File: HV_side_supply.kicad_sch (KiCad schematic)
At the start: 34 parts, among them U103 LM217MDT, U104 LM217MDT

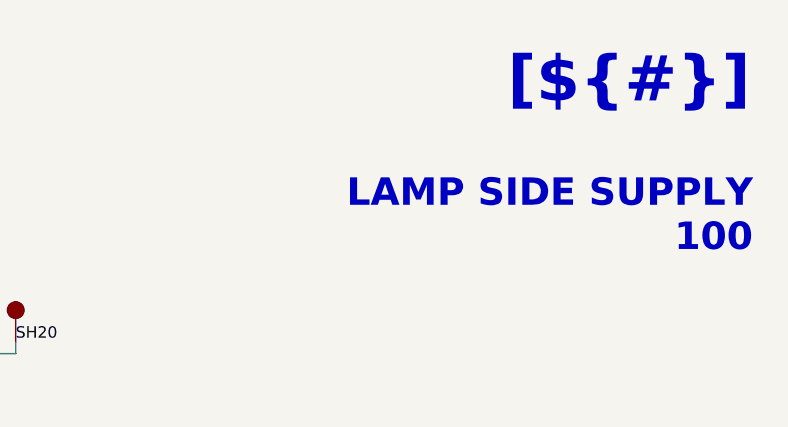
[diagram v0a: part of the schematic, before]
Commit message: Reworked sheet titles
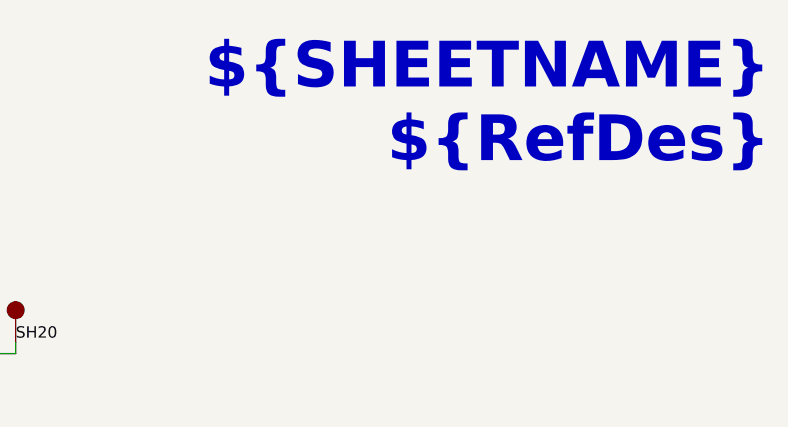
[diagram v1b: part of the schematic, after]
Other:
- note removed: "LAMP SIDE SUPPLY 100"
- title: (none) -> ${SHEETNAME}
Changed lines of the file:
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@@
 	(paper "A4")
 	(title_block
+		(title "${SHEETNAME}")
 		(date "2025-01-12")
 	)
@@
 		)
 	)
-	(text "LAMP SIDE SUPPLY\n100"
+	(text_box "${SHEETNAME}\n${RefDes}"
 		(exclude_from_sim no)
-		(at 277.495 35.56 0)
-		(effects
-			(font
-				(size 3.048 3.048)
-				(thickness 0.4064)
-				(bold yes)
-				(color 0 0 255 1)
-			)
-			(justify right)
-		)
-	)
-	(text_box "[${#}] ${TITLE}"
-		(exclude_from_sim no)
-		(at 181.61 13.97 0)
-		(size 101.6 12.7)
-		(margins 5.9999 5.9999 5.9999 5.9999)
+		(at 228.6 15.24 0)
+		(size 53.34 15.24)
+		(margins 2.54 1.27 2.54 1.27)
 		(stroke
 			(width -0.0001)

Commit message: Added PCB
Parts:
- PS101: footprint Personal:DCDC_converter_Hilink -> Personal:Hilink_no_courtyard
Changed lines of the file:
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@@
 	(title_block
 		(title "${SHEETNAME}")
-		(date "2025-01-12")
+		(date "2025-07-04")
 	)
 	(rectangle
@@
 		(at 228.6 15.24 0)
 		(size 53.34 15.24)
-		(margins 2.54 1.27 2.54 1.27)
+		(margins 1.27 1.27 1.27 1.27)
 		(stroke
 			(width -0.0001)
@@
 			)
 		)
-		(property "Description" ""
+		(property "Description" "Local power symbol (source), cosmetic use only"
 			(at 195.58 49.53 0)
 			(effects
@@
 			)
 		)
-		(property "Description" ""
+		(property "Description" "Local power symbol (sink), cosmetic use only"
 			(at 88.9 49.53 0)
 			(effects
@@
 			)
 		)
-		(property "Description" ""
+		(property "Description" "Local power symbol (sink), cosmetic use only"
 			(at 160.02 90.17 0)
 			(effects
@@
 			)
 		)
-		(property "Description" ""
+		(property "Description" "Local power symbol (source), cosmetic use only"
 			(at 143.51 49.53 0)
 			(effects
@@
 	)
 	(symbol
-		(lib_name "Cosmetic_PWR_4")
 		(lib_id "personal:Cosmetic_PWR")
 		(at 33.02 46.99 0)
@@
 			)
 		)
-		(property "Description" ""
+		(property "Description" "Local power symbol (sink), cosmetic use only"
 			(at 33.02 46.99 0)
 			(effects
@@
 	)
 	(symbol
-		(lib_name "Cosmetic_PWR_4")
 		(lib_id "personal:Cosmetic_PWR")
 		(at 86.36 54.61 0)
@@
 			)
 		)
-		(property "Description" ""
+		(property "Description" "Local power symbol (sink), cosmetic use only"
 			(at 86.36 54.61 0)
 			(effects
@@
 			)
 		)
-		(property "Description" ""
+		(property "Description" "Local power symbol (source), cosmetic use only"
 			(at 33.02 31.75 0)
 			(effects
@@
 			)
 		)
-		(property "Description" ""
+		(property "Description" "Local power symbol (source), cosmetic use only"
 			(at 195.58 106.68 0)
 			(effects
@@
 			)
 		)
-		(property "Description" ""
+		(property "Description" "Local power symbol (source), cosmetic use only"
 			(at 33.02 24.13 0)
 			(effects
@@
 			)
 		)
-		(property "Description" ""
+		(property "Description" "Local power symbol (sink), cosmetic use only"
 			(at 149.86 90.17 0)
 			(effects
@@
 			)
 		)
-		(property "Footprint" "Personal:DCDC_converter_Hilink"
+		(property "Footprint" "Personal:Hilink_no_courtyard"
 			(at 106.68 60.96 0)
 			(effects
@@
 	)
 	(symbol
-		(lib_name "Cosmetic_PWR_4")
 		(lib_id "personal:Cosmetic_PWR")
 		(at 33.02 39.37 0)
@@
 			)
 		)
-		(property "Description" ""
+		(property "Description" "Local power symbol (sink), cosmetic use only"
 			(at 33.02 39.37 0)
 			(effects

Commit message: Readme updated
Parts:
- PS101: footprint Personal:Hilink_no_courtyard -> Converter_ACDC:Converter_ACDC_Hi-Link_HLK-5Mxx
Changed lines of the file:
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@@
 			)
 		)
-		(property "Footprint" "Personal:Hilink_no_courtyard"
+		(property "Footprint" "Converter_ACDC:Converter_ACDC_Hi-Link_HLK-5Mxx"
 			(at 106.68 60.96 0)
 			(effects

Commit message: updating BOM info
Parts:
- C101, C103, C105, R101, R102, R103, R104, R106: Manufacturer (none) -> Generic
- C102, C104: Manufacturer (none) -> CCTC; Manufacturer Part Number (none) -> TCC0603X7R104K500CT
- PS101: Manufacturer (none) -> Hilink; Manufacturer Part Number (none) -> HLK-5M24
- U103, U104: Manufacturer (none) -> ST; Manufacturer Part Number (none) -> LM217MDT

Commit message: Checked. Preparing release
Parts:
- PS101: footprint Converter_ACDC:Converter_ACDC_Hi-Link_HLK-5Mxx -> Personal:Hilink_no_courtyard
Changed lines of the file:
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@@
 			)
 		)
-		(property "Footprint" "Converter_ACDC:Converter_ACDC_Hi-Link_HLK-5Mxx"
+		(property "Footprint" "Personal:Hilink_no_courtyard"
 			(at 106.68 60.96 0)
 			(effects
